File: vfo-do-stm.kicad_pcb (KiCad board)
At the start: 2 copper layers, 88.5 x 52.5 mm, 35 parts, among them J1 SWIM, J2 DC_in, J3 LO, J4 VFO, SW1 SW_FreqMinus, SW2 SW_FreqPlus, SW3 SW_Band, SW4 SW_Res, SW5 SW_NRST, U1 L7805, U2 LE33CD, U3 STM8S208C8, U4 LE33CD, U5 LE33CD, U6 Si5351A-B-GT, U7 TCA9535DBR, Y1 24MHz

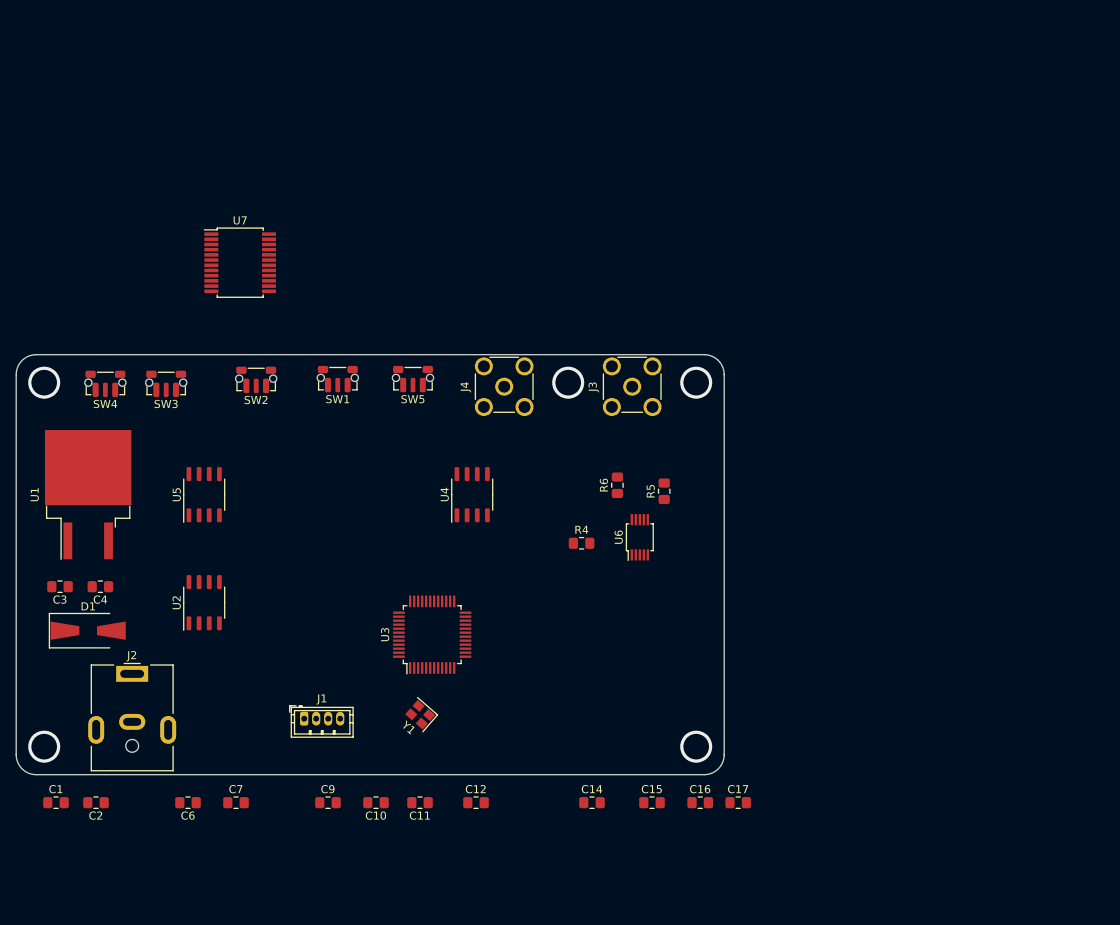
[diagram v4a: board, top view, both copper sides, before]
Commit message: Répartition des éléments du schéma en feuilles hiérarchiques
petites modifs du pcb
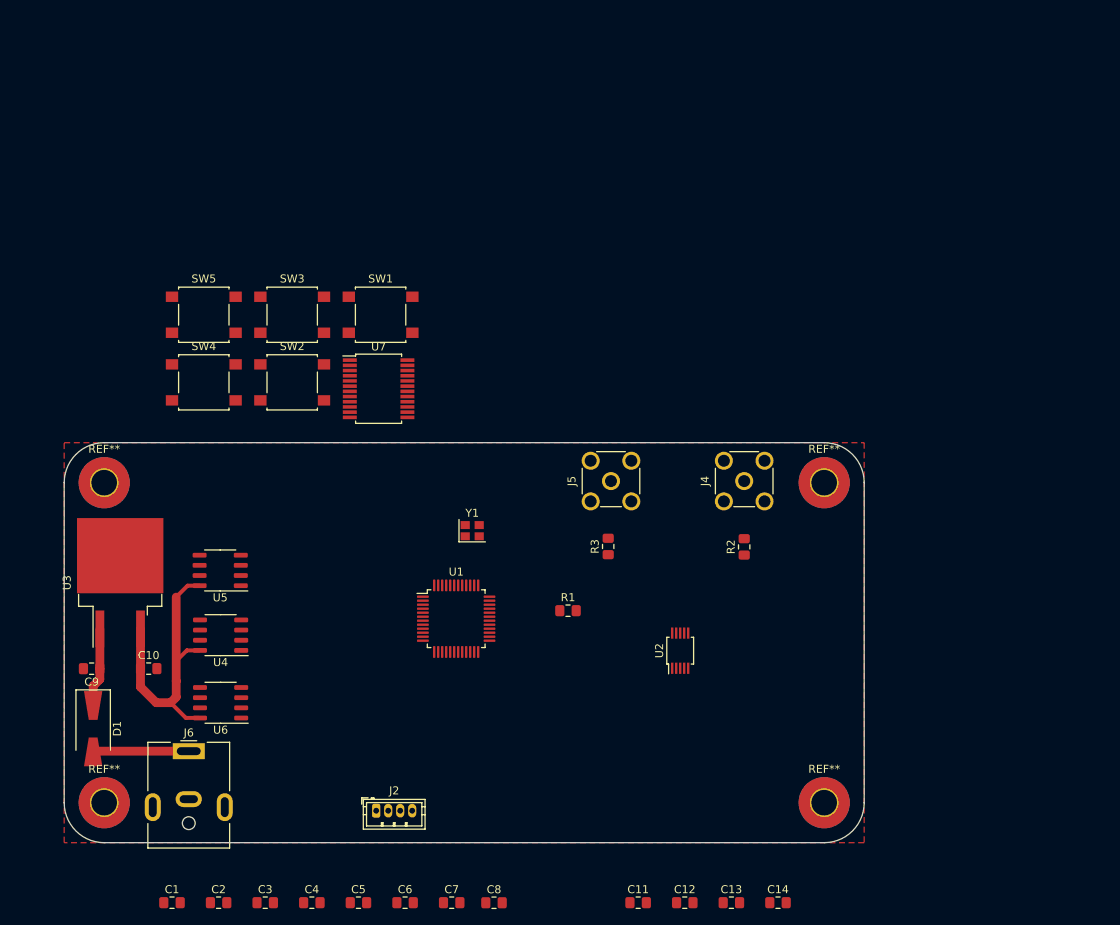
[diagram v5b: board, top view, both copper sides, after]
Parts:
- removed C15: 0.47µF, Capacitor_SMD:C_0805_2012Metric_Pad1.15x1.40mm_HandSolder
- removed C16, C17: 20pF, Capacitor_SMD:C_0805_2012Metric_Pad1.15x1.40mm_HandSolder
- removed J1: SWIM, Connector_JST:JST_ZH_B4B-ZR_1x04_P1.50mm_Vertical
- removed J3: LO, Connector_Coaxial:SMA_Molex_73251-2200_Horizontal
- removed R4, R5, R6: 0Ω, Resistor_SMD:R_0805_2012Metric_Pad1.15x1.40mm_HandSolder
- added C13: 0.1µF, Capacitor_SMD:C_0805_2012Metric_Pad1.15x1.40mm_HandSolder, F.Cu at (143.4, 148.5)
- added C5: 0.47µF, Capacitor_SMD:C_0805_2012Metric_Pad1.15x1.40mm_HandSolder, F.Cu at (96.8, 148.5)
- added C8: 10µF, Capacitor_SMD:C_0805_2012Metric_Pad1.15x1.40mm_HandSolder, F.Cu at (113.7, 148.5)
- added J5: VFO, Connector_Coaxial:SMA_Molex_73251-2200_Horizontal, F.Cu at (128.3, 95.8)
- added J6: DC_in, Connector_BarrelJack:BarrelJack_CUI_PJ-063AH_Horizontal, F.Cu at (75.6, 129.6)
- added R1: 0Ω, Resistor_SMD:R_0805_2012Metric_Pad1.15x1.40mm_HandSolder, F.Cu at (123.0, 112.0)
- added R2: 0Ω, Resistor_SMD:R_0805_2012Metric_Pad1.15x1.40mm_HandSolder, F.Cu at (145.0, 104.0)
- added R3: 0Ω, Resistor_SMD:R_0805_2012Metric_Pad1.15x1.40mm_HandSolder, F.Cu at (128.0, 104.0)
- added REF**: MountingHole_3.2mm_M3_Pad_TopBottom, MountingHole:MountingHole_3.2mm_M3_Pad_TopBottom, F.Cu at (155.0, 96.0)
- added REF**: MountingHole_3.2mm_M3_Pad_TopBottom, MountingHole:MountingHole_3.2mm_M3_Pad_TopBottom, F.Cu at (65.0, 96.0)
- added REF**: MountingHole_3.2mm_M3_Pad_TopBottom, MountingHole:MountingHole_3.2mm_M3_Pad_TopBottom, F.Cu at (155.0, 136.0)
- added REF**: MountingHole_3.2mm_M3_Pad_TopBottom, MountingHole:MountingHole_3.2mm_M3_Pad_TopBottom, F.Cu at (65.0, 136.0)
- C1: value 0.1µF -> 20pF
- C10: value 100nF -> 0.1µF
- C14: value 0.47µF -> 10µF
- C2: value 10µF -> 20pF
- C3: value 0.33µF -> 1µF
- C4: value 0.1µF -> 100nF
- C6: value 0.1µF -> 0.47µF
- C7: value 10µF -> 0.1µF
- C9: value 1µF -> 0.33µF
- J2: value DC_in -> SWIM; footprint Connector_BarrelJack:BarrelJack_CUI_PJ-063AH_Horizontal -> Connector_JST:JST_ZH_B4B-ZR_1x04_P1.50mm_Vertical
- J4: value VFO -> LO
- SW1: value SW_FreqMinus -> BP1; footprint Button_Switch_SMD:SW_Push_1P1T-MP_NO_Horizontal_Alps_SKRTLAE010 -> Button_Switch_SMD:SW_SPST_B3S-1000
- SW2: value SW_FreqPlus -> BP2; footprint Button_Switch_SMD:SW_Push_1P1T-MP_NO_Horizontal_Alps_SKRTLAE010 -> Button_Switch_SMD:SW_SPST_B3S-1000
- SW3: value SW_Band -> BP3; footprint Button_Switch_SMD:SW_Push_1P1T-MP_NO_Horizontal_Alps_SKRTLAE010 -> Button_Switch_SMD:SW_SPST_B3S-1000
- SW4: value SW_Res -> BP4; footprint Button_Switch_SMD:SW_Push_1P1T-MP_NO_Horizontal_Alps_SKRTLAE010 -> Button_Switch_SMD:SW_SPST_B3S-1000
- SW5: footprint Button_Switch_SMD:SW_Push_1P1T-MP_NO_Horizontal_Alps_SKRTLAE010 -> Button_Switch_SMD:SW_SPST_B3S-1000
- U1: value L7805 -> STM8S208C8; footprint Package_TO_SOT_SMD:TO-263-2 -> Package_QFP:LQFP-48_7x7mm_P0.5mm
- U2: value LE33CD -> Si5351A-B-GT; footprint Package_SO:SO-8_3.9x4.9mm_P1.27mm -> Package_SO:MSOP-10_3x3mm_P0.5mm
- U3: value STM8S208C8 -> L7805; footprint Package_QFP:LQFP-48_7x7mm_P0.5mm -> Package_TO_SOT_SMD:TO-263-2
- U6: value Si5351A-B-GT -> LE33CD; footprint Package_SO:MSOP-10_3x3mm_P0.5mm -> Package_SO:SO-8_3.9x4.9mm_P1.27mm
- moved U2 59.8 mm to (137.0, 117.0)
- moved U6 56.3 mm to (79.5, 123.5), turned to 180 degrees
- moved U1 48.5 mm to (109.0, 113.0), turned to 0 degrees
- moved C4 47.5 mm to (91.0, 148.5), turned to 0 degrees
- moved C3 47.1 mm to (85.1, 148.5), turned to 0 degrees
- moved U3 39.5 mm to (67.0, 108.5)
- moved U4 36.0 mm to (79.5, 115.1), turned to 180 degrees
- moved J2 35.0 mm to (99.0, 137.0)
- moved C9 34.0 mm to (63.4, 119.2), turned to 180 degrees
- moved C10 33.0 mm to (70.6, 119.2), turned to 0 degrees
- moved J4 32.2 mm to (145.0, 95.8)
- moved C11 30.0 mm to (131.7, 148.5), turned to 0 degrees
- moved C6 29.9 mm to (102.6, 148.5), turned to 0 degrees
- moved C7 29.7 mm to (108.4, 148.5)
- moved C12 28.9 mm to (137.6, 148.5)
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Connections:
- C1 pad 1: /Net_5.5V -> Net-(C1-Pad1)
- C10 pad 1: NRST -> /Alimentation/Net_5.5V
- C11 pad 1: /Net_5.5V -> /Alimentation/Net_5.5V
- C12 pad 1: 3.3CLK -> /Alimentation/3.3_LCD
- C2 pad 1: 3.3MCU -> Net-(C2-Pad1)
- C4 pad 1: /Net_5.5V -> NRST
- C6 pad 1: /Net_5.5V -> 3.3CLK
- C7 pad 1: 3.3LCD -> /Alimentation/Net_5.5V
- D1 pad 1: Net-(C3-Pad1) -> Net-(C9-Pad1)
- J2 pad 1: Net-(D1-Pad2) -> /Alimentation/3.3_MCU
- J2 pad 2: GND -> Net-(J2-Pad2)
- SW1 pad 2: Net-(SW1-Pad2) -> GND
- SW2 pad 2: Net-(SW2-Pad2) -> GND
- SW3 pad 2: Net-(SW3-Pad2) -> GND
- SW4 pad 2: Net-(SW4-Pad2) -> GND
- SW5 pad 2: NRST -> Net-(SW5-Pad2)
- U1 pad 1: Net-(C3-Pad1) -> NRST
- U1 pad 2: GND -> Net-(C1-Pad1)
- U1 pad 3: /Net_5.5V -> Net-(C2-Pad1)
- U2 pad 1: 3.3MCU -> 3.3CLK
- U2 pad 2: GND -> (no net)
- U2 pad 3: GND -> (no net)
- U2 pad 4: Net-(U2-Pad4) -> I²C_SCL
- U2 pad 5: GND -> I²C_SDA
- U2 pad 6: GND -> Net-(R2-Pad1)
- U2 pad 7: GND -> 3.3CLK
- U2 pad 8: /Net_5.5V -> GND
- U3 pad 1: NRST -> Net-(C9-Pad1)
- U3 pad 2: Net-(C16-Pad1) -> GND
- U3 pad 3: Net-(C17-Pad1) -> /Alimentation/Net_5.5V
- U4 pad 1: 3.3LCD -> /Alimentation/3.3_MCU
- U4 pad 4: Net-(U4-Pad4) -> (no net)
- U4 pad 5: INH_LCD -> GND
- U4 pad 8: /Net_5.5V -> /Alimentation/Net_5.5V
- U5 pad 1: 3.3CLK -> /Alimentation/3.3_LCD
- U5 pad 4: Net-(U5-Pad4) -> (no net)
- U5 pad 5: INH_CLK -> INH_LCD
- U5 pad 8: /Net_5.5V -> /Alimentation/Net_5.5V
- U6 pad 2: Net-(U6-Pad2) -> GND
- U6 pad 3: Net-(U6-Pad3) -> GND
- U6 pad 4: I²C_SCL -> (no net)
- U6 pad 5: I²C_SDA -> INH_CLK
- U6 pad 6: Net-(R5-Pad1) -> GND
- U6 pad 7: 3.3CLK -> GND
- U6 pad 8: GND -> /Alimentation/Net_5.5V
- U7 pad 1: Net-(U7-Pad1) -> (no net)
- U7 pad 10: Net-(U7-Pad10) -> (no net)
- U7 pad 11: Net-(U7-Pad11) -> (no net)
- U7 pad 12: Net-(U7-Pad12) -> (no net)
- U7 pad 13: Net-(U7-Pad13) -> (no net)
- U7 pad 14: Net-(U7-Pad14) -> (no net)
- U7 pad 15: Net-(U7-Pad15) -> (no net)
- U7 pad 16: Net-(U7-Pad16) -> (no net)
- U7 pad 17: Net-(U7-Pad17) -> (no net)
- U7 pad 18: Net-(U7-Pad18) -> (no net)
- U7 pad 19: Net-(U7-Pad19) -> (no net)
- U7 pad 2: Net-(U7-Pad2) -> (no net)
- U7 pad 20: Net-(U7-Pad20) -> (no net)
- U7 pad 21: Net-(U7-Pad21) -> (no net)
- U7 pad 22: Net-(U7-Pad22) -> (no net)
- U7 pad 23: Net-(U7-Pad23) -> (no net)
- U7 pad 24: Net-(U7-Pad24) -> (no net)
- U7 pad 3: Net-(U7-Pad3) -> (no net)
- U7 pad 8: Net-(U7-Pad8) -> (no net)
- U7 pad 9: Net-(U7-Pad9) -> (no net)
- Y1 pad 1: Net-(C17-Pad1) -> Net-(C2-Pad1)
- Y1 pad 3: Net-(C16-Pad1) -> Net-(C1-Pad1)
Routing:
- net /Alimentation/Net_5.5V: track 0.00 -> 39.4 mm
- net Net-(D1-Pad2): track 0.00 -> 12.0 mm
- net Net-(C9-Pad1): track 0.00 -> 9.92 mm
- net GND: vias 5 -> 0
- added copper zone on F.Cu, net GND
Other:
- board size 88.5 x 52.5 mm -> 100 x 50 mm
- net class Alim added: clearance 0.5, trace_width 1.1, via_dia 1.6, via_drill 0.8
